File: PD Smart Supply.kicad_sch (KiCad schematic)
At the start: 20 parts, among them U1 CH224A, U2 TPS560430XDBVR, U3 STM32G071CBT6

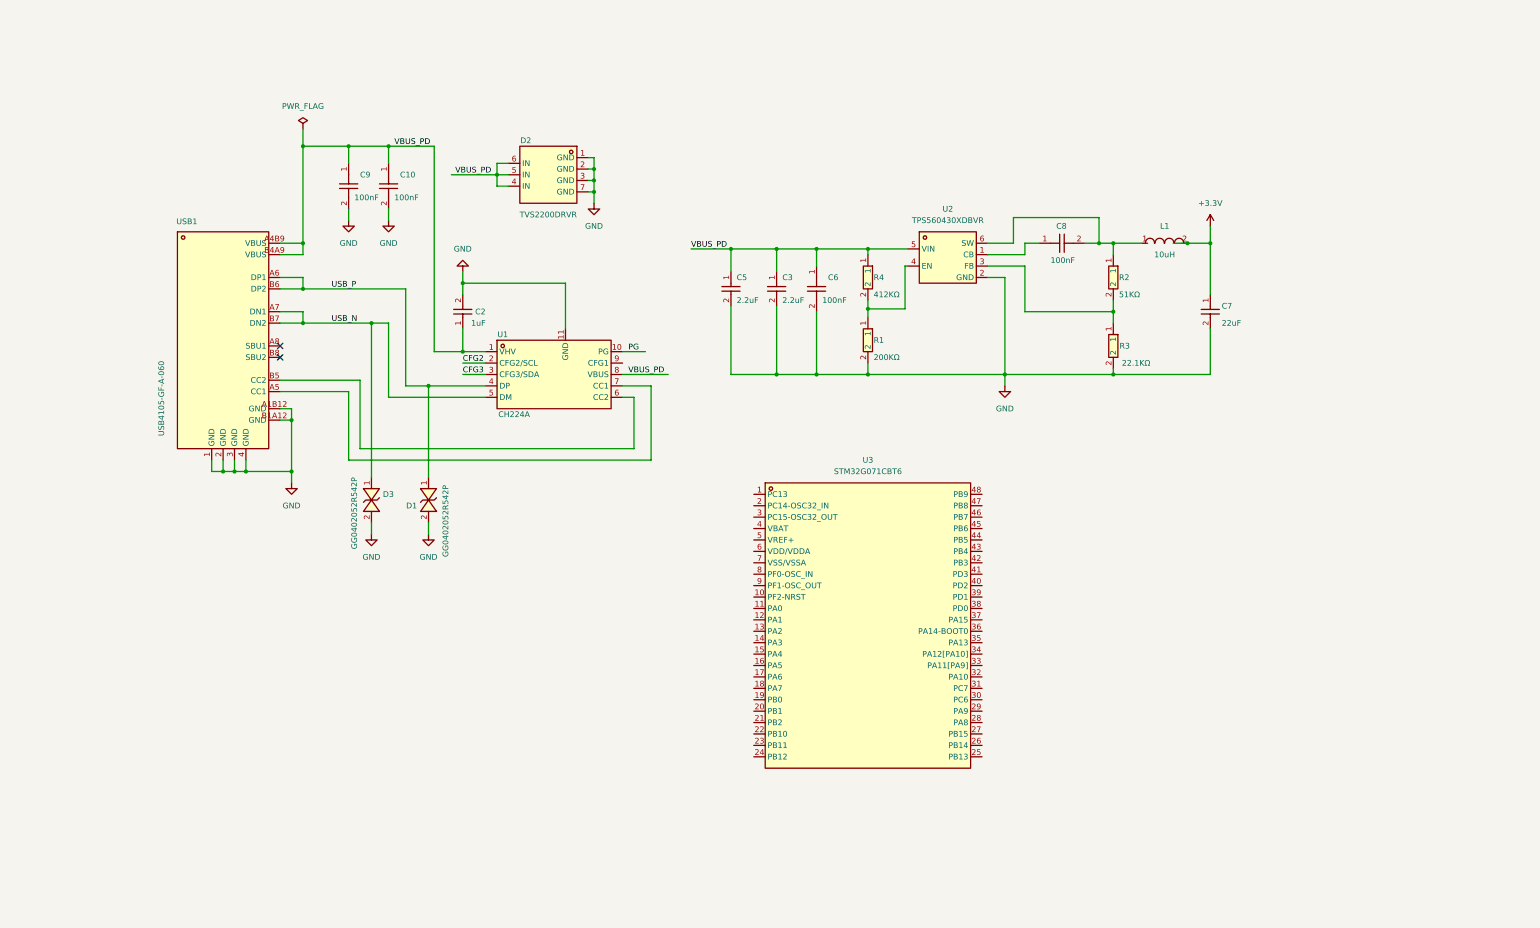
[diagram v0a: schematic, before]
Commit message: feat: add MCU, SWD, OLED, error LED, and eFuse circuitry
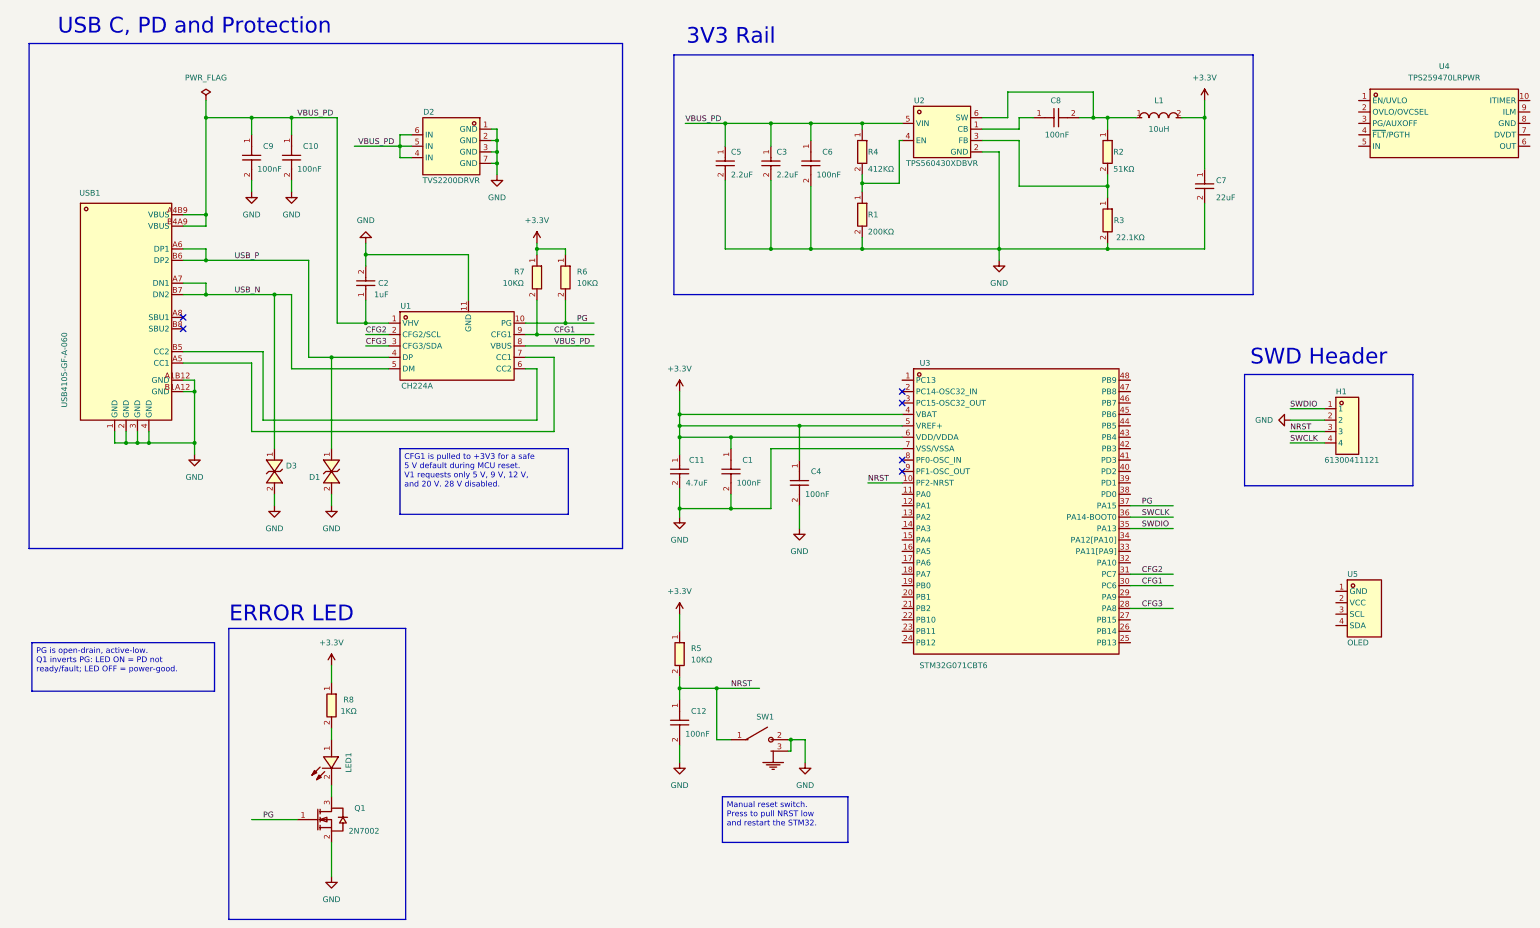
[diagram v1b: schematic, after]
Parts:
- added C1, C12, C4: 100nF, easyeda2kicad:C0603, symbol PD Smart Supply:CC0603KRX7R9BB104
- added C11: 4.7uF, easyeda2kicad:C0805, symbol PD Smart Supply:CL21A475KAQNNNE
- added H1: 61300411121, easyeda2kicad:HDR-TH_4P-P2.54-V-M-1, symbol PD Smart Supply:61300411121
- added LED1: KT-0603R, easyeda2kicad:LED-SMD_L1.6-W0.8-R-RD, symbol PD Smart Supply:KT-0603R
- added Q1: 2N7002, easyeda2kicad:SOT-23-3_L2.9-W1.3-P1.90-LS2.4-BR, symbol PD Smart Supply:2N7002
- added R5, R6, R7: 10KΩ, easyeda2kicad:R0402, symbol PD Smart Supply:0402WGF1002TCE
- added R8: 1KΩ, easyeda2kicad:R0402, symbol PD Smart Supply:0402WGF1001TCE
- added SW1: Switch, easyeda2kicad:SW-SMD_XYECONN_TSC01-TBW0FH3.5, symbol PD Smart Supply:TSC01-TBW0FH3.5
- added U4: TPS259470LRPWR, easyeda2kicad:VQFN-10_L2.0-W2.0-P0.45-TL, symbol PD Smart Supply:TPS259470LRPWR
- added U5: OLED, easyeda2kicad:OLED-TH_L27.8-W27.2-P2.54_C9900033791, symbol PD Smart Supply:HS96L03W2C03
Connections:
- net +3.3V: now also U3.4 (VBAT), U3.5 (VREF+), U3.6 (VDD/VDDA), C1.1, C11.1, C4.1, R5.1, R6.1, R7.1, R8.1
- net CFG2: now also U3.31 (PC7)
- net CFG3: now also U3.28 (PA8)
- net GND: now also U3.7 (VSS/VSSA), C1.2, C11.2, C12.2, C4.2, H1.2, Q1.2, SW1.2, SW1.3
- net PG: now also U3.37 (PA15), Q1.1, R6.2
- net NRST: now reaches U3.10 (PF2-NRST)
- net NRST: now also C12.1, H1.3, R5.2, SW1.1
- net CFG1: now reaches U3.30 (PC6)
- net CFG1: now also U1.9 (CFG1), R7.2
- net SWDIO: now reaches U3.35 (PA13)
- net SWDIO: now also H1.1
- net SWCLK: now reaches U3.36 (PA14-BOOT0)
- net SWCLK: now also H1.4
- new net: LED1.1, R8.2
- new net: LED1.2, Q1.3
- no-connect marks 2 -> 6
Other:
- note added: "3V3 Rail"
- note added: "ERROR LED"
- note added: "SWD Header"
- note added: "USB C, PD and Protection"
- moved on the sheet: C10, C2, C3, C5, C6, C7, C8, C9, D1, D2, D3, L1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
